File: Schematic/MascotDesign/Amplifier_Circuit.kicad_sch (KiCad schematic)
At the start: 31 parts, among them J1 Screw_Terminal_01x02, J2 Screw_Terminal_01x03, J3 AudioJack2, J4 Screw_Terminal_01x02, U4 TPA3116D2DAD

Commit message: fix some minor differences in amplifier circuit
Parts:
- C11, C12: value C -> 1 uF
- J1: value Screw_Terminal_01x02 -> Speaker 8R
- J4: value Screw_Terminal_01x02 -> Audio in
- L1, L2: value L -> 10 uH
- R1: value R -> 13.2 R
- R2: value 3.3R -> 13.2 R
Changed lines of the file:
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@@
 			)
 		)
-		(property "Value" "R"
+		(property "Value" "13.2 R"
 			(at 237.49 107.9499 0)
 			(effects
@@
 			)
 		)
-		(property "Value" "L"
+		(property "Value" "10 uH"
 			(at 193.04 107.95 90)
 			(effects
@@
 			)
 		)
-		(property "Value" "3.3R"
+		(property "Value" "13.2 R"
 			(at 237.49 85.0899 0)
 			(effects
@@
 			)
 		)
-		(property "Value" "C"
+		(property "Value" "1 uF"
 			(at 200.66 105.4099 0)
 			(effects
@@
 			)
 		)
-		(property "Value" "Screw_Terminal_01x02"
+		(property "Value" "Audio in"
 			(at 24.13 54.61 0)
 			(effects
@@
 			)
 		)
-		(property "Value" "C"
+		(property "Value" "1 uF"
 			(at 200.66 88.8999 0)
 			(effects
@@
 			)
 		)
-		(property "Value" "L"
+		(property "Value" "10 uH"
 			(at 193.04 77.47 90)
 			(effects
@@
 			)
 		)
-		(property "Value" "Screw_Terminal_01x02"
+		(property "Value" "Speaker 8R"
 			(at 260.35 96.5199 0)
 			(effects

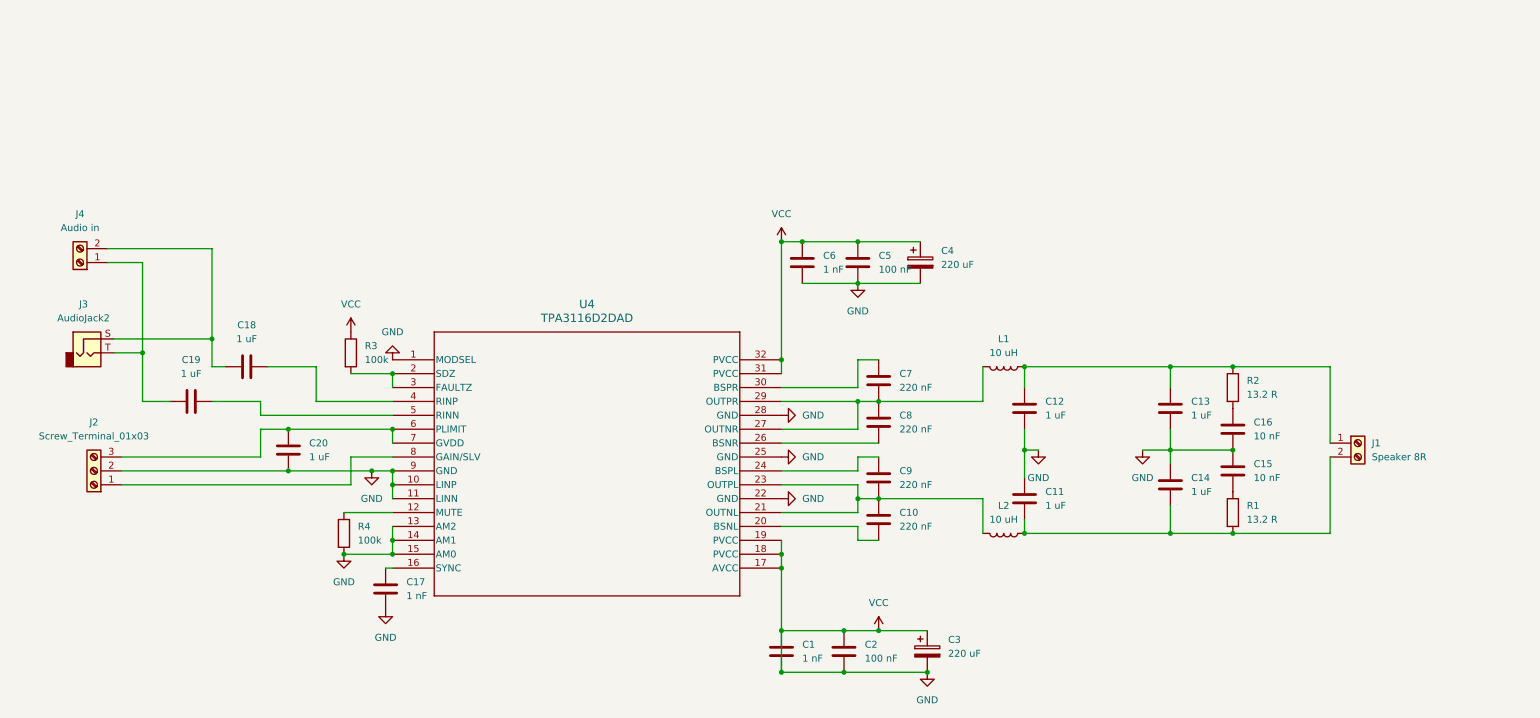
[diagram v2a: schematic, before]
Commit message: Assign footprints and begin PCB layout
Need to check the ECE shop to see what parts we have on hand before we get too far into this, but still.
It's a start.
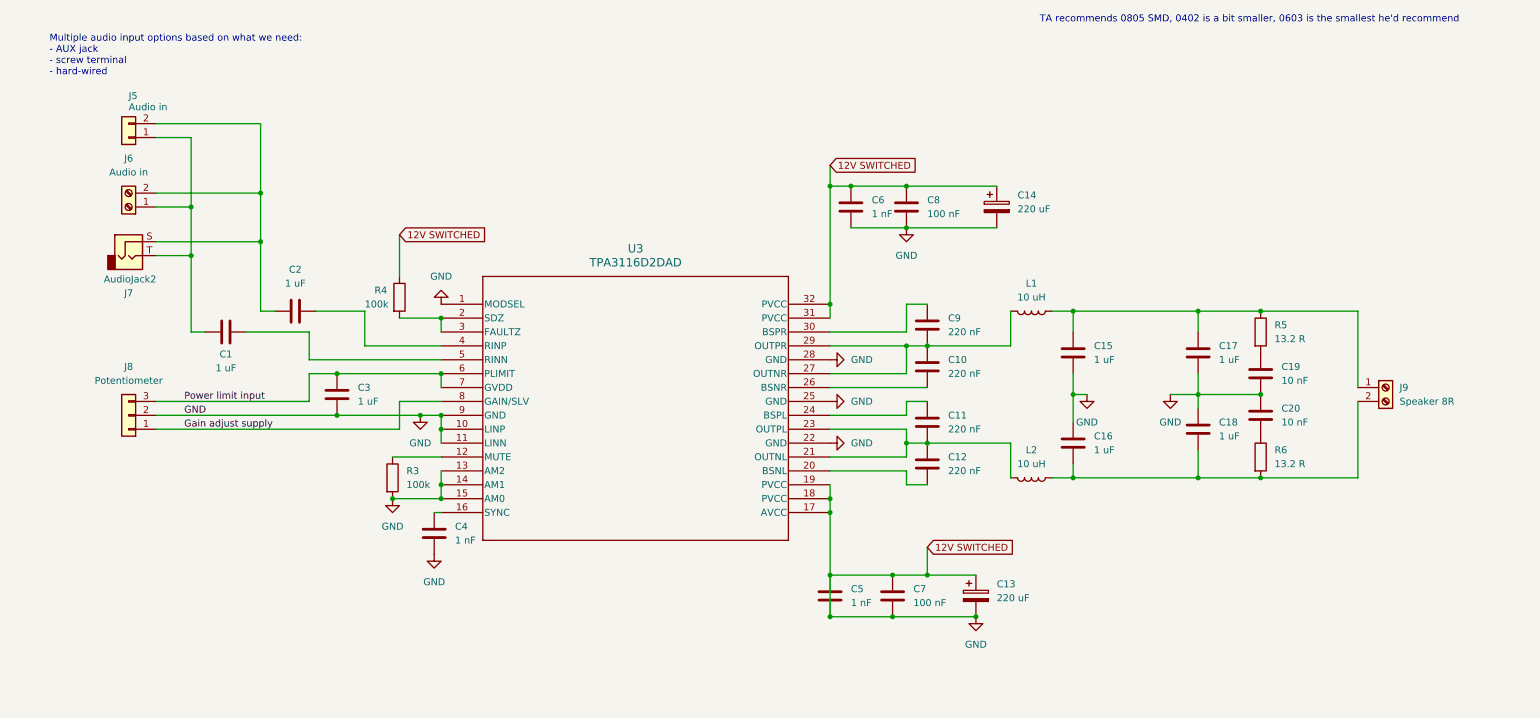
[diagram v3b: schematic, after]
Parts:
- removed J2: Screw_Terminal_01x03, symbol Connector:Screw_Terminal_01x03
- added J5: Audio in, Connector_PinHeader_2.54mm:PinHeader_1x02_P2.54mm_Vertical, symbol Connector_Generic:Conn_01x02
- added J8: Potentiometer, Connector_PinHeader_2.54mm:PinHeader_1x03_P2.54mm_Vertical, symbol Connector_Generic:Conn_01x03
- C1: renamed from C19; footprint (none) -> Capacitor_THT:C_Disc_D5.0mm_W2.5mm_P5.00mm
- C10: renamed from C8; footprint (none) -> Capacitor_THT:C_Disc_D5.0mm_W2.5mm_P5.00mm
- C11: renamed from C9; footprint (none) -> Capacitor_THT:C_Disc_D5.0mm_W2.5mm_P5.00mm
- C12: renamed from C10; footprint (none) -> Capacitor_THT:C_Disc_D5.0mm_W2.5mm_P5.00mm
- C13: renamed from C3; footprint (none) -> Capacitor_THT:CP_Radial_D5.0mm_P2.50mm
- C14: renamed from C4; footprint (none) -> Capacitor_THT:CP_Radial_D5.0mm_P2.50mm
- C15: renamed from C12; footprint (none) -> Capacitor_THT:C_Disc_D5.0mm_W2.5mm_P5.00mm
- C16: renamed from C11; footprint (none) -> Capacitor_THT:C_Disc_D5.0mm_W2.5mm_P5.00mm
- C17: renamed from C13; footprint (none) -> Capacitor_THT:C_Disc_D5.0mm_W2.5mm_P5.00mm
- C18: renamed from C14; footprint (none) -> Capacitor_THT:C_Disc_D5.0mm_W2.5mm_P5.00mm
- C19: renamed from C16; footprint (none) -> Capacitor_THT:C_Disc_D5.0mm_W2.5mm_P5.00mm
- C2: renamed from C18; footprint (none) -> Capacitor_THT:C_Disc_D5.0mm_W2.5mm_P5.00mm
- C20: renamed from C15; footprint (none) -> Capacitor_THT:C_Disc_D5.0mm_W2.5mm_P5.00mm
- C3: renamed from C20; footprint (none) -> Capacitor_THT:C_Disc_D5.0mm_W2.5mm_P5.00mm
- C4: renamed from C17; footprint (none) -> Capacitor_THT:C_Disc_D5.0mm_W2.5mm_P5.00mm
- C5: renamed from C1; footprint (none) -> Capacitor_THT:C_Disc_D5.0mm_W2.5mm_P5.00mm
- C6: footprint (none) -> Capacitor_THT:C_Disc_D5.0mm_W2.5mm_P5.00mm
- C7: renamed from C2; footprint (none) -> Capacitor_THT:C_Disc_D5.0mm_W2.5mm_P5.00mm
- C8: renamed from C5; footprint (none) -> Capacitor_THT:C_Disc_D5.0mm_W2.5mm_P5.00mm
- C9: renamed from C7; footprint (none) -> Capacitor_THT:C_Disc_D5.0mm_W2.5mm_P5.00mm
- J6: renamed from J4; footprint (none) -> TerminalBlock_RND:TerminalBlock_RND_205-00001_1x02_P5.00mm_Horizontal
- J9: renamed from J1; footprint (none) -> TerminalBlock_RND:TerminalBlock_RND_205-00001_1x02_P5.00mm_Horizontal
- L1, L2: footprint (none) -> Inductor_THT:L_Radial_D6.0mm_P4.00mm
- R3: renamed from R4; footprint (none) -> Resistor_THT:R_Axial_DIN0207_L6.3mm_D2.5mm_P7.62mm_Horizontal
- R4: renamed from R3; footprint (none) -> Resistor_THT:R_Axial_DIN0207_L6.3mm_D2.5mm_P7.62mm_Horizontal
- R5: renamed from R2; footprint (none) -> Resistor_THT:R_Axial_DIN0207_L6.3mm_D2.5mm_P7.62mm_Horizontal
- R6: renamed from R1; footprint (none) -> Resistor_THT:R_Axial_DIN0207_L6.3mm_D2.5mm_P7.62mm_Horizontal
- U3: renamed from U4; footprint DAD32_TEX -> My_Library:SOP65P810X115-32N
- renumbered J3 to J7
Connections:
- net GND: now also J8.2 (Pin_2)
- net Gain adjust supply: now reaches U3.8 (GAIN/SLV)
- net Gain adjust supply: now also J8.1 (Pin_1)
- net Power limit input: now reaches C3.2, U3.6 (PLIMIT), U3.7 (GVDD)
- net Power limit input: now also J8.3 (Pin_3)
- net at C2.2, J6.2 (Pin_2), J7.S: now also J5.2 (Pin_2)
- net at C1.2, J6.1 (Pin_1), J7.T: now also J5.1 (Pin_1)
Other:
- note added: "Multiple audio input options based on what we need: - AUX jack - screw terminal - hard-wired"
- note added: "TA recommends 0805 SMD, 0402 is a bit smaller, 0603 is the smallest he'd recommend"
- title: (none) -> Amplifier subsystem
- moved on the sheet: C1, C10, C11, C12, C13, C14, C15, C16, C17, C18, C19, C2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

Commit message: Work on CAD and schematics
Got most of the components modeled for reference, now arranging them and creating brackets
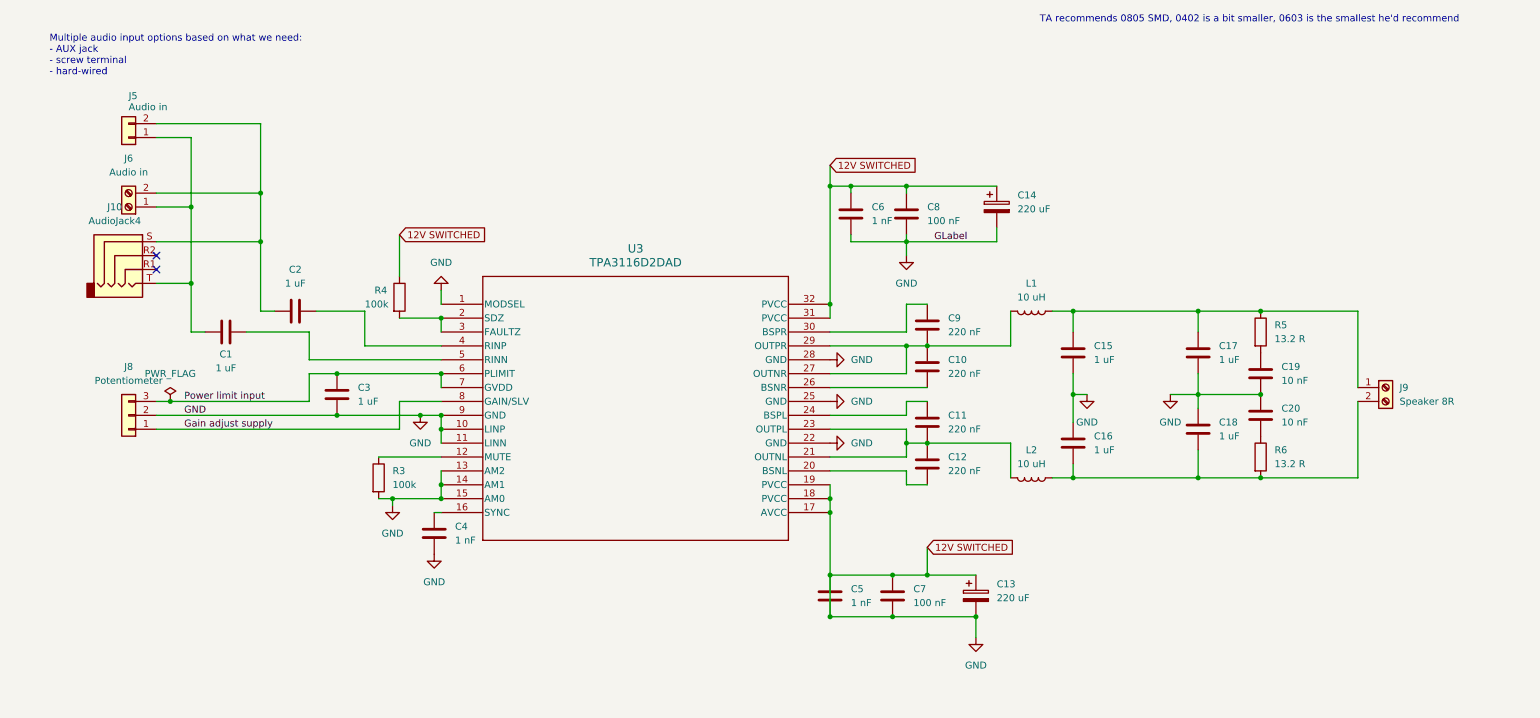
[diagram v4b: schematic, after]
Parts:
- removed J7: AudioJack2, symbol Connector_Audio:AudioJack2
- added J10: AudioJack4, My_Library:PJ-320A, symbol Connector_Audio:AudioJack4
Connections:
- net at C1.2, J5.1 (Pin_1), J6.1 (Pin_1): now also J10.T
- net at C2.2, J5.2 (Pin_2), J6.2 (Pin_2): now also J10.S
- no-connect marks 0 -> 2
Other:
- moved on the sheet: C6, C8, R3

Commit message: Do PCB layout
I need to check our cap footprints to make sure we got the right ones.
Other than that, the PCB should be mostly routed.
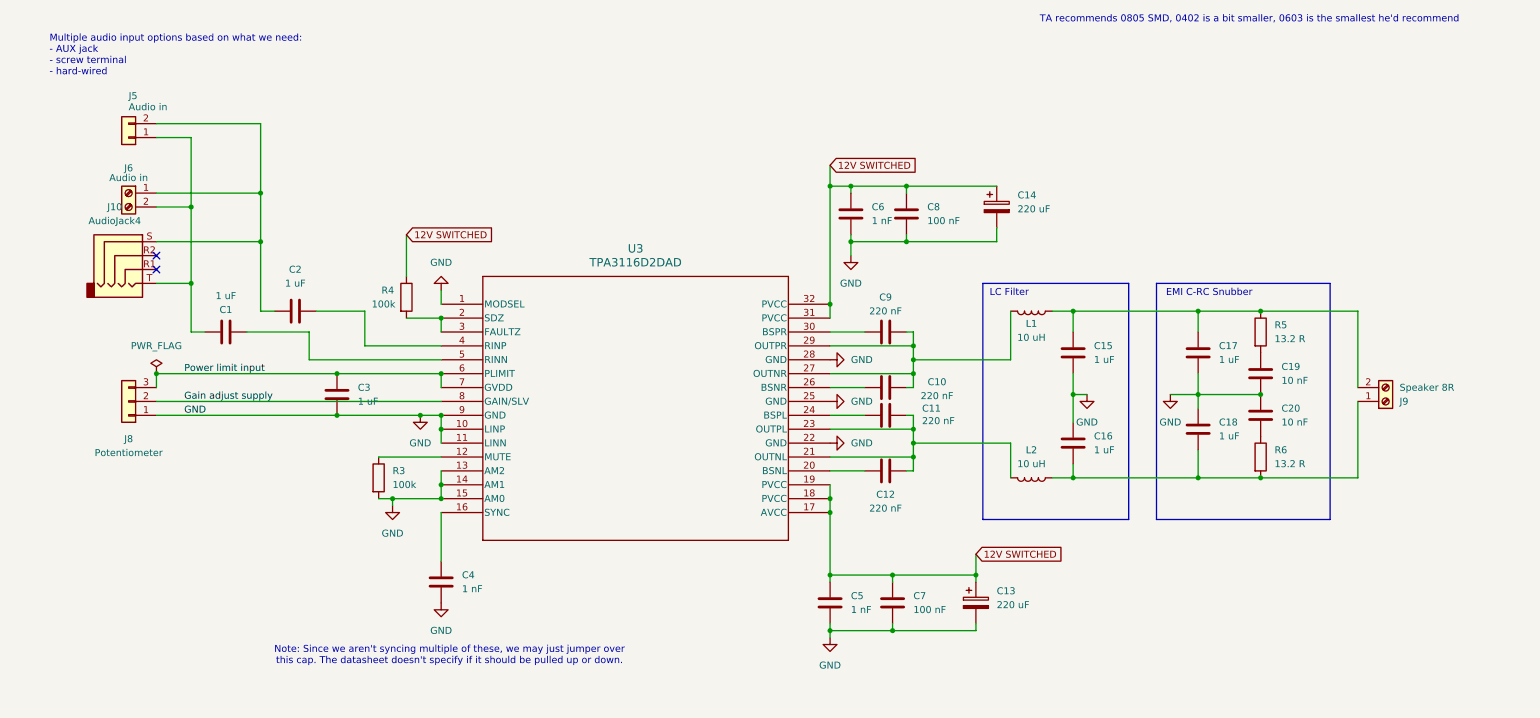
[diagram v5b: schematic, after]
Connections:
- net GND: now also J8.1 (Pin_1); no longer C13.1, C14.1, C5.1, C6.1, C7.1, C8.1, J8.2 (Pin_2), R4.1, U3.17 (AVCC), U3.18 (PVCC), U3.19 (PVCC), U3.31 (PVCC), U3.32 (PVCC)
- net Gain adjust supply: now also J8.2 (Pin_2); no longer J8.1 (Pin_1)
- net at C16.1, C18.1, L2.1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: now also J9.1 (Pin_1); no longer J9.2 (Pin_2)
- net at C11.1, L2.2, U3.21 (OUTNL)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: now also C12.1; no longer C12.2
- net at C15.2, C17.2, L1.1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: now also J9.2 (Pin_2); no longer J9.1 (Pin_1)
- net at C2.2, J10.S, J5.2 (Pin_2): now also J6.1 (Pin_1); no longer J6.2 (Pin_2)
- net at J10.T, J5.1 (Pin_1): now also C1.1, J6.2 (Pin_2); no longer C1.2, J6.1 (Pin_1)
- net at U3.20 (BSNL): now also C12.2; no longer C12.1
- net at U3.26 (BSNR): now also C10.2; no longer C10.1
- net at C9.1, L1.2, U3.27 (OUTNR)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: now also C10.1; no longer C10.2
- net at U3.5 (RINN): now also C1.2; no longer C1.1
- new net 12V SWITCHED: C13.1, C14.1, C5.1, C6.1, C7.1, C8.1, R4.1, U3.17 (AVCC), U3.18 (PVCC), U3.19 (PVCC), U3.31 (PVCC), U3.32 (PVCC)
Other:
- note added: "EMI C-RC Snubber"
- note added: "LC Filter"
- note added: "Note: Since we aren't syncing multiple of these, we may just jumper over this cap. The datasheet doesn't specify if it should be pulled up or down."
- moved on the sheet: C1, C10, C11, C12, C13, C4, C5, C7, C9, J6, J8, R4

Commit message: update PCB and mounting brackets
give PCB the correct footprints for the parts we have and add more mounting brackets for the 3D model
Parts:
- C1, C15, C16, C17, C18, C2, C3: footprint Capacitor_THT:C_Disc_D5.0mm_W2.5mm_P5.00mm -> Capacitor_THT:C_Disc_D4.7mm_W2.5mm_P5.00mm
- C10, C11, C12, C9: footprint Capacitor_THT:C_Disc_D5.0mm_W2.5mm_P5.00mm -> Capacitor_THT:C_Disc_D5.0mm_W2.5mm_P2.50mm
- C13, C14: footprint Capacitor_THT:CP_Radial_D5.0mm_P2.50mm -> Capacitor_THT:CP_Radial_D10.0mm_P5.00mm
- C19, C20, C4, C5, C6, C7, C8: footprint Capacitor_THT:C_Disc_D5.0mm_W2.5mm_P5.00mm -> Capacitor_THT:C_Disc_D3.0mm_W2.0mm_P2.50mm
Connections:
- net at C2.2, J10.S, J5.2 (Pin_2): now also J6.2 (Pin_2); no longer J6.1 (Pin_1)
- net at C1.1, J10.T, J5.1 (Pin_1): now also J6.1 (Pin_1); no longer J6.2 (Pin_2)
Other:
- moved on the sheet: J6
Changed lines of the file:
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@@
 			)
 		)
-		(property "Footprint" "Capacitor_THT:C_Disc_D5.0mm_W2.5mm_P5.00mm"
+		(property "Footprint" "Capacitor_THT:C_Disc_D3.0mm_W2.0mm_P2.50mm"
 			(at 162.2552 127 0)
 			(effects
@@
 			)
 		)
-		(property "Footprint" "Capacitor_THT:C_Disc_D5.0mm_W2.5mm_P5.00mm"
+		(property "Footprint" "Capacitor_THT:C_Disc_D3.0mm_W2.0mm_P2.50mm"
 			(at 166.0652 55.88 0)
 			(effects
@@
 			)
 		)
-		(property "Footprint" "Capacitor_THT:C_Disc_D5.0mm_W2.5mm_P5.00mm"
+		(property "Footprint" "Capacitor_THT:C_Disc_D3.0mm_W2.0mm_P2.50mm"
 			(at 173.6852 127 0)
 			(effects
@@
 			)
 		)
-		(property "Footprint" "Capacitor_THT:C_Disc_D5.0mm_W2.5mm_P5.00mm"
+		(property "Footprint" "Capacitor_THT:C_Disc_D5.0mm_W2.5mm_P2.50mm"
 			(at 167.64 89.8652 0)
 			(effects
@@
 			)
 		)
-		(property "Footprint" "Capacitor_THT:C_Disc_D5.0mm_W2.5mm_P5.00mm"
+		(property "Footprint" "Capacitor_THT:C_Disc_D4.7mm_W2.5mm_P5.00mm"
 			(at 227.6348 87.63 0)
 			(effects
@@
 			)
 		)
-		(property "Footprint" "Capacitor_THT:C_Disc_D5.0mm_W2.5mm_P5.00mm"
+		(property "Footprint" "Capacitor_THT:C_Disc_D4.7mm_W2.5mm_P5.00mm"
 			(at 70.1548 81.28 0)
 			(effects
@@
 			)
 		)
-		(property "Footprint" "Capacitor_THT:C_Disc_D5.0mm_W2.5mm_P5.00mm"
+		(property "Footprint" "Capacitor_THT:C_Disc_D4.7mm_W2.5mm_P5.00mm"
 			(at 204.7748 90.17 0)
 			(effects
@@
 			)
 		)
-		(property "Footprint" "Capacitor_THT:C_Disc_D5.0mm_W2.5mm_P5.00mm"
+		(property "Footprint" "Capacitor_THT:C_Disc_D4.7mm_W2.5mm_P5.00mm"
 			(at 227.6348 73.66 0)
 			(effects
@@
 			)
 		)
-		(property "Footprint" "Capacitor_THT:C_Disc_D5.0mm_W2.5mm_P5.00mm"
+		(property "Footprint" "Capacitor_THT:C_Disc_D3.0mm_W2.0mm_P2.50mm"
 			(at 239.0648 85.09 0)
 			(effects
@@
 			)
 		)
-		(property "Footprint" "Capacitor_THT:C_Disc_D5.0mm_W2.5mm_P5.00mm"
+		(property "Footprint" "Capacitor_THT:C_Disc_D5.0mm_W2.5mm_P2.50mm"
 			(at 167.64 100.0252 0)
 			(effects
@@
 			)
 		)
-		(property "Footprint" "Capacitor_THT:C_Disc_D5.0mm_W2.5mm_P5.00mm"
+		(property "Footprint" "Capacitor_THT:C_Disc_D3.0mm_W2.0mm_P2.50mm"
 			(at 176.2252 55.88 0)
 			(effects
@@
 			)
 		)
-		(property "Footprint" "Capacitor_THT:C_Disc_D5.0mm_W2.5mm_P5.00mm"
+		(property "Footprint" "Capacitor_THT:C_Disc_D3.0mm_W2.0mm_P2.50mm"
 			(at 91.1352 123.19 0)
 			(effects
@@
 			)
 		)
-		(property "Footprint" "Capacitor_THT:C_Disc_D5.0mm_W2.5mm_P5.00mm"
+		(property "Footprint" "Capacitor_THT:C_Disc_D3.0mm_W2.0mm_P2.50mm"
 			(at 239.0648 77.47 0)
 			(effects
@@
 			)
 		)
-		(property "Footprint" "Capacitor_THT:CP_Radial_D5.0mm_P2.50mm"
+		(property "Footprint" "Capacitor_THT:CP_Radial_D10.0mm_P5.00mm"
 			(at 188.9252 127 0)
 			(effects
@@
 			)
 		)
-		(property "Footprint" "Capacitor_THT:C_Disc_D5.0mm_W2.5mm_P5.00mm"
+		(property "Footprint" "Capacitor_THT:C_Disc_D4.7mm_W2.5mm_P5.00mm"
 			(at 59.69 70.8152 0)
 			(effects
@@
 			)
 		)
-		(property "Footprint" "Capacitor_THT:C_Disc_D5.0mm_W2.5mm_P5.00mm"
+		(property "Footprint" "Capacitor_THT:C_Disc_D5.0mm_W2.5mm_P2.50mm"
 			(at 167.64 84.7852 0)
 			(effects
@@
 	(symbol
 		(lib_id "Connector:Screw_Terminal_01x02")
-		(at 33.02 48.26 0)
-		(mirror y)
+		(at 33.02 50.8 180)
 		(unit 1)
 		(exclude_from_sim no)
@@
 		(dnp no)
 		(property "Reference" "J6"
-			(at 33.02 43.688 0)
+			(at 33.02 42.926 0)
 			(effects
 				(font
@@
 		)
 		(property "Value" "Audio in"
-			(at 33.02 45.466 0)
+			(at 33.02 45.212 0)
 			(effects
 				(font
@@
 		)
 		(property "Footprint" "TerminalBlock_RND:TerminalBlock_RND_205-00001_1x02_P5.00mm_Horizontal"
-			(at 33.02 48.26 0)
+			(at 33.02 50.8 0)
 			(effects
 				(font
@@
 		)
 		(property "Datasheet" "~"
-			(at 33.02 48.26 0)
+			(at 33.02 50.8 0)
 			(effects
 				(font
@@
 		)
 		(property "Description" "Generic screw terminal, single row, 01x02, script generated (kicad-library-utils/schlib/autogen/connector/)"
-			(at 33.02 48.26 0)
+			(at 33.02 50.8 0)
 			(effects
 				(font
@@
 			)
 		)
-		(property "Footprint" "Capacitor_THT:C_Disc_D5.0mm_W2.5mm_P5.00mm"
+		(property "Footprint" "Capacitor_THT:C_Disc_D4.7mm_W2.5mm_P5.00mm"
 			(at 204.7748 73.66 0)
 			(effects
@@
 			)
 		)
-		(property "Footprint" "Capacitor_THT:CP_Radial_D5.0mm_P2.50mm"
+		(property "Footprint" "Capacitor_THT:CP_Radial_D10.0mm_P5.00mm"
 			(at 192.7352 54.61 0)
 			(effects
@@
 			)
 		)
-		(property "Footprint" "Capacitor_THT:C_Disc_D5.0mm_W2.5mm_P5.00mm"
+		(property "Footprint" "Capacitor_THT:C_Disc_D5.0mm_W2.5mm_P2.50mm"
 			(at 167.64 74.6252 0)
 			(effects
@@
 			)
 		)
-		(property "Footprint" "Capacitor_THT:C_Disc_D5.0mm_W2.5mm_P5.00mm"
+		(property "Footprint" "Capacitor_THT:C_Disc_D4.7mm_W2.5mm_P5.00mm"
 			(at 54.61 72.6948 0)
 			(effects

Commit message: ensure board passes DRC errors
not warnings though. Those are mostly just silkscreen overlaps.
We need to put something funny on the silkscreen yet.
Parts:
- C4, C5, C6, C7, C8: footprint Capacitor_THT:C_Disc_D3.0mm_W2.0mm_P2.50mm -> Capacitor_THT:C_Disc_D3.0mm_W1.6mm_P2.50mm
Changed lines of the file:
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@@
 			)
 		)
-		(property "Footprint" "Capacitor_THT:C_Disc_D3.0mm_W2.0mm_P2.50mm"
+		(property "Footprint" "Capacitor_THT:C_Disc_D3.0mm_W1.6mm_P2.50mm"
 			(at 162.2552 127 0)
 			(effects
@@
 			)
 		)
-		(property "Footprint" "Capacitor_THT:C_Disc_D3.0mm_W2.0mm_P2.50mm"
+		(property "Footprint" "Capacitor_THT:C_Disc_D3.0mm_W1.6mm_P2.50mm"
 			(at 166.0652 55.88 0)
 			(effects
@@
 			)
 		)
-		(property "Footprint" "Capacitor_THT:C_Disc_D3.0mm_W2.0mm_P2.50mm"
+		(property "Footprint" "Capacitor_THT:C_Disc_D3.0mm_W1.6mm_P2.50mm"
 			(at 173.6852 127 0)
 			(effects
@@
 			)
 		)
-		(property "Footprint" "Capacitor_THT:C_Disc_D3.0mm_W2.0mm_P2.50mm"
+		(property "Footprint" "Capacitor_THT:C_Disc_D3.0mm_W1.6mm_P2.50mm"
 			(at 176.2252 55.88 0)
 			(effects
@@
 			)
 		)
-		(property "Footprint" "Capacitor_THT:C_Disc_D3.0mm_W2.0mm_P2.50mm"
+		(property "Footprint" "Capacitor_THT:C_Disc_D3.0mm_W1.6mm_P2.50mm"
 			(at 91.1352 123.19 0)
 			(effects
